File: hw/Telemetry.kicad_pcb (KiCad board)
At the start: 4 copper layers, 100 x 82 mm, 96 parts, among them J101 VS1053 EXP, J102 BOOT0, J103 SPORT, J104 SBUS, J105 USB_B_Micro, J106 UART_EXP, J201 Conn_01x02, J301 Conn_01x02, J302 Conn_01x02, J401 Conn_01x02, J402 Conn_01x02, J403 Conn_01x02, J404 Conn_01x02, J405 Conn_01x02, J406 Conn_01x02, J407 Conn_01x02, J408 Conn_01x02, J409 SERVO_OUT, Q201 AO3401A, Q401 IRLML6344TRPBF, Q402 IRLML6344TRPBF, Q403 IRLML6344TRPBF, Q404 IRLZ44N, Q405 IRLML6344TRPBF, Q406 IRLML6344TRPBF, Q407 IRLML6344TRPBF, Q408 IRLZ44N, SW101 SW_Push, U101 STM32F303CBx, U201 AP1501-K5, U202 RT6200, U301 LF50_TO220, U302 ACS770xCB-100U-PSF, U303 OP179GRT, U304 ACS770xCB-100U-PSF, U305 OP179GRT, X101 TXC-7C

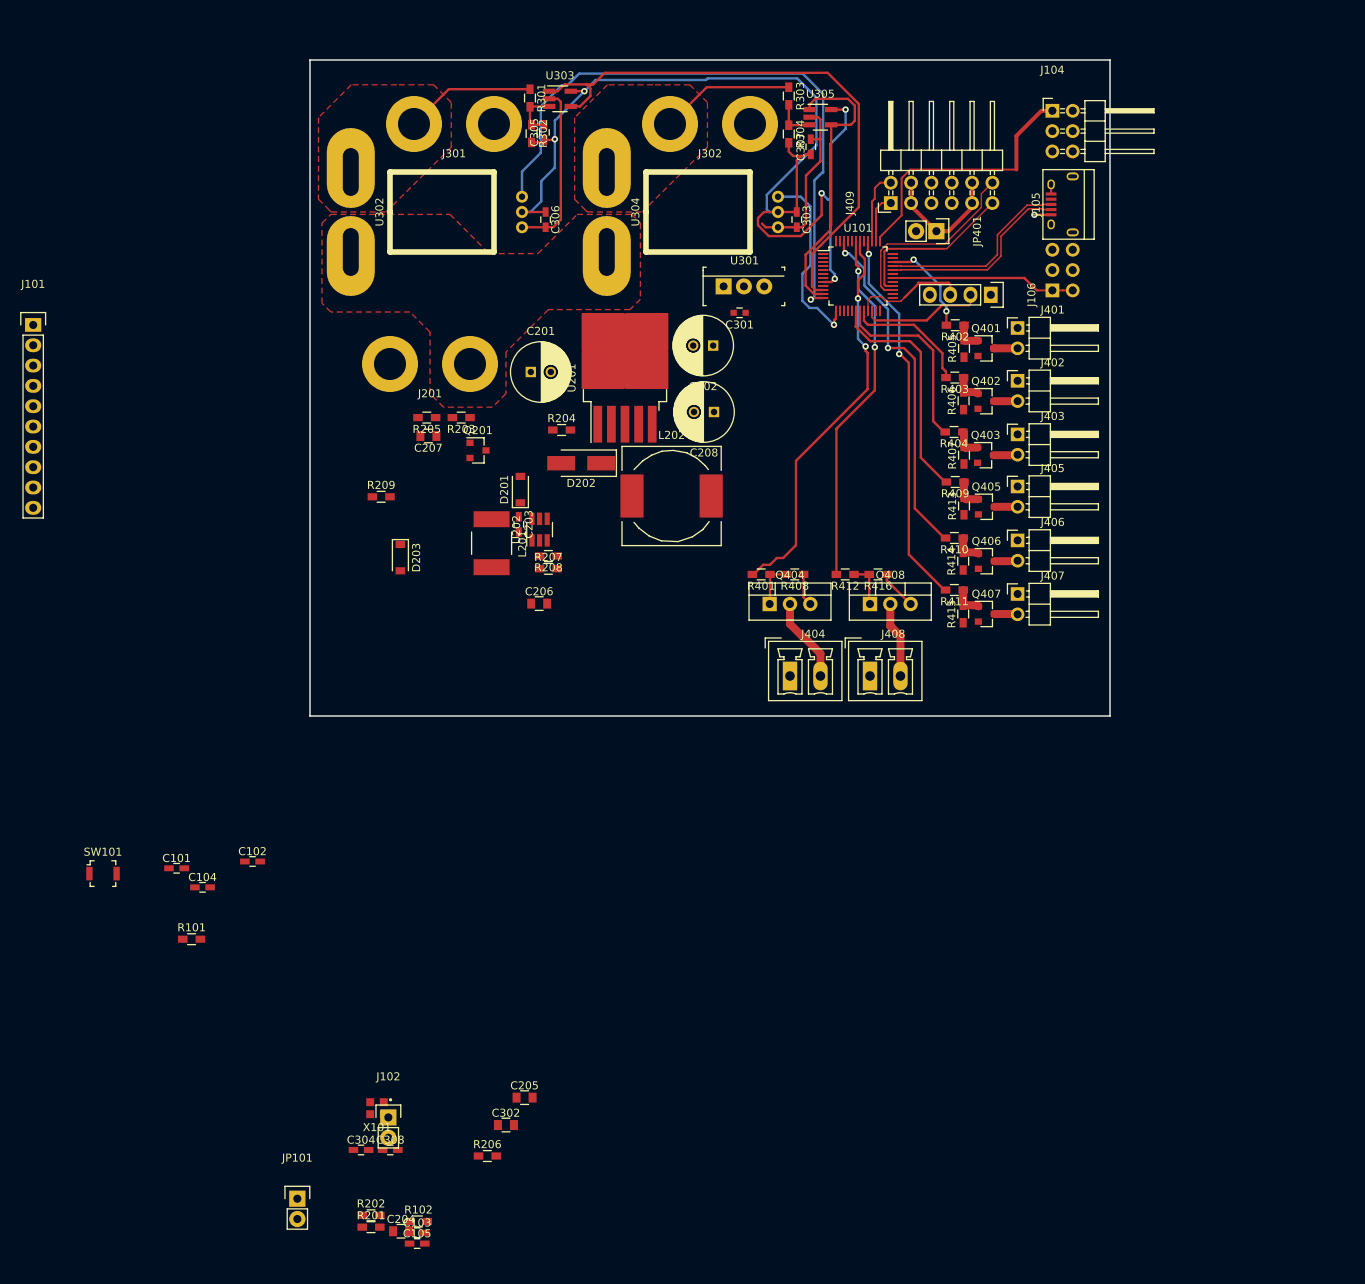
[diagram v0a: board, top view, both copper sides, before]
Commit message: Continued layout Setup USB device CDC
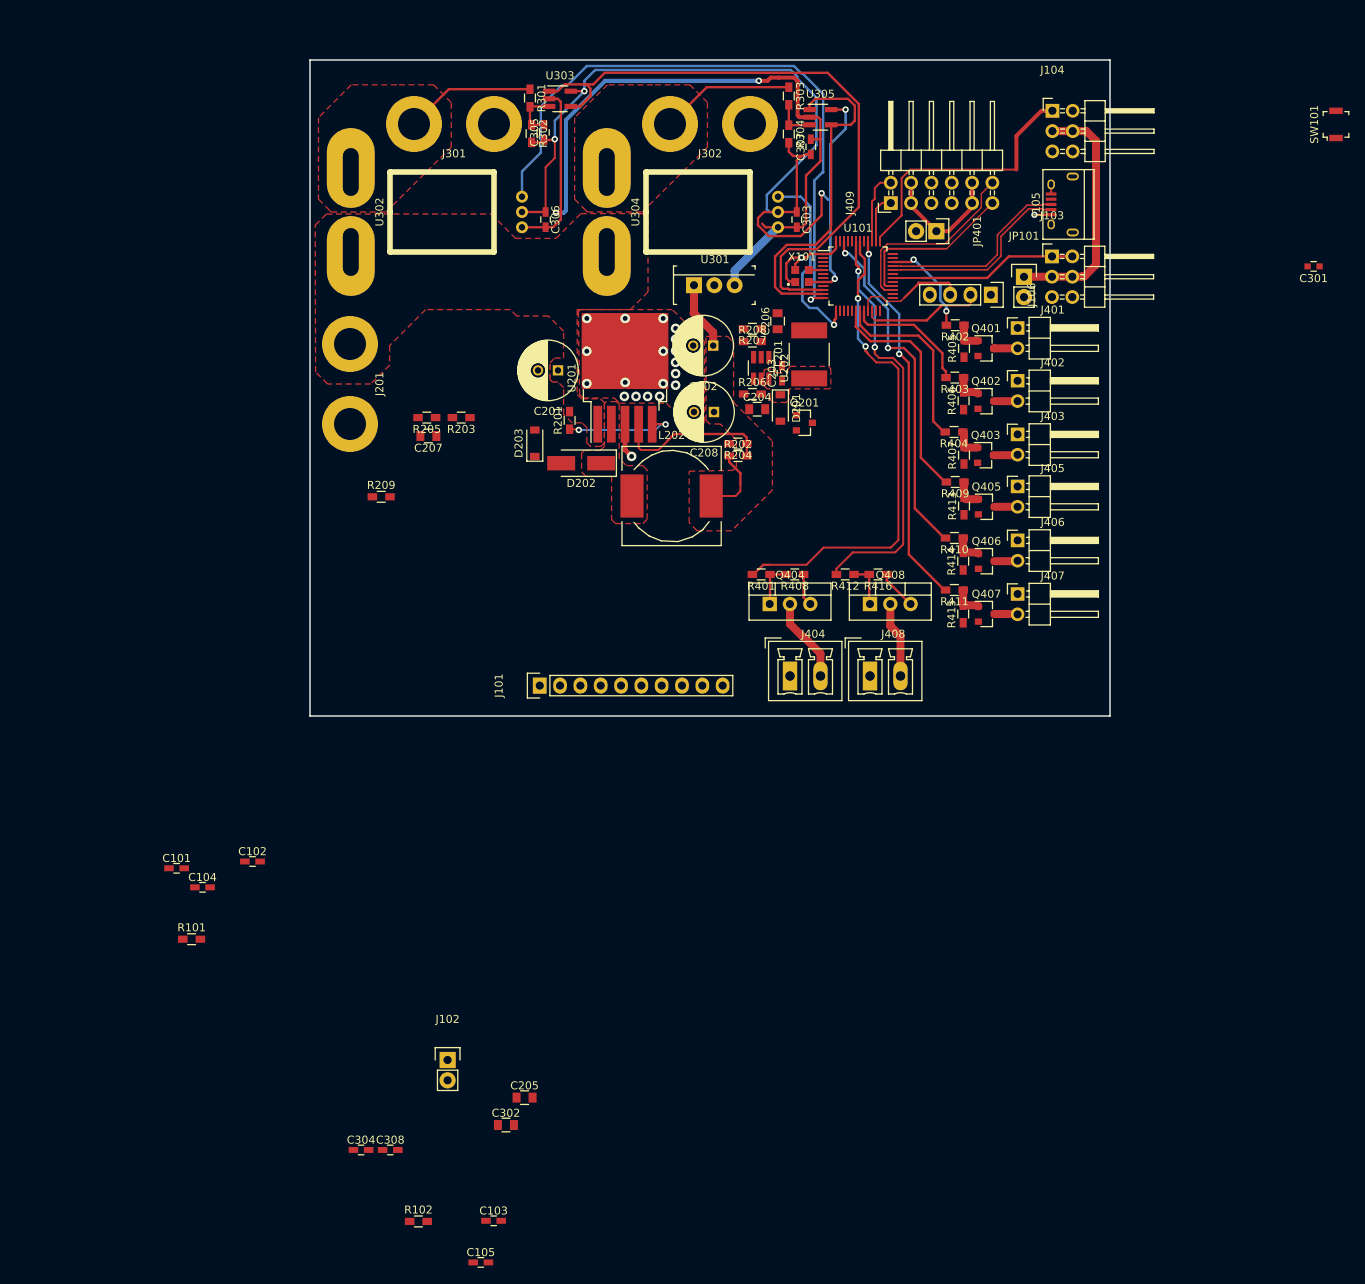
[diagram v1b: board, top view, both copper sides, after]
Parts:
- J103: moved to F.Cu
- moved SW101 180.4 mm to (188.2, 46.0), turned to 90 degrees
- moved JP101 146.7 mm to (149.2, 65.1)
- moved X101 116.8 mm to (121.5, 65.0), turned to 180 degrees
- moved C204 112.0 mm to (115.9, 81.7)
- moved R202 105.4 mm to (113.5, 87.5)
- moved R201 103.9 mm to (92.5, 83.0), turned to 90 degrees
- moved R206 100.9 mm to (115.3, 79.8)
- moved J101 77.7 mm to (88.7, 116.2), turned to 90 degrees
- moved C301 72.0 mm to (185.4, 63.8)
- moved C206 46.2 mm to (118.5, 70.7), turned to 90 degrees
- moved L201 46.2 mm to (122.4, 74.8), turned to 90 degrees
- moved Q201 40.9 mm to (121.8, 83.3)
- moved R207 39.4 mm to (115.3, 71.6), turned to 180 degrees
- moved C203 37.9 mm to (119.0, 77.2), turned to 90 degrees
- moved R208 37.0 mm to (115.3, 73.2), turned to 0 degrees
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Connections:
- U101 pad 1: Net-(R101-Pad1) -> +3V3
- U101 pad 7: (no net) -> Net-(R101-Pad1)
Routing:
- net +5VA: track 43.9 -> 103.9 mm, vias 0 -> 2
- net Net-(J103-Pad3): track 0.00 -> 31.1 mm
- net Net-(R202-Pad2): track 0.00 -> 19.9 mm
- net VCC: track 2.09 -> 19.6 mm
- net Net-(R201-Pad1): track 0.00 -> 14.1 mm, vias 0 -> 2
- net +3V3: track 0.00 -> 13.0 mm, vias 0 -> 1
- net HC_OUT1: track 49.8 -> 61.2 mm
- net ESC1_VOLTAGE_OUT: track 72.7 -> 80.4 mm
- net ESC2_VOLTAGE_OUT: track 36.1 -> 43.8 mm
- net HC_OUT2: track 44.6 -> 51.7 mm
- net GND: track 144.5 -> 150.6 mm, vias 5 -> 24
- net Net-(U101-Pad5): track 0.00 -> 1.83 mm
- net ESC1_CURRENT_OUT: track 78.5 -> 79.3 mm
- added copper zone on F.Cu, net GND
- added copper zone on F.Cu, net Net-(C203-Pad1)
- added copper zone on F.Cu, net Net-(D202-Pad1)
- added copper zone on F.Cu, net VCC

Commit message: Layout improvements
Signed-off-by: findersee <aki.kuusela@findersee.fi>
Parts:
- removed C207: 100n, Capacitors_SMD:C_0805
- removed C305, C308: 100n, Capacitors_SMD:C_0603_HandSoldering
- removed D203: D_Schottky, Diodes_SMD:D_SOD-123
- added C309: 2u2, Capacitors_SMD:C_0805, F.Cu at (106.6, 66.1)
- added Q202: AO3401A, digikey-footprints:SOT-23-3, F.Cu at (112.2, 100.9)
- added Q203: IRLML6344TRPBF, digikey-footprints:SOT-23-3, F.Cu at (87.8, 84.2)
- added Q204: IRLML6344TRPBF, digikey-footprints:SOT-23-3, F.Cu at (83.4, 83.2)
- added R210: 100k, Resistors_SMD:R_0603_HandSoldering, F.Cu at (112.1, 103.8)
- added R211: 10k, Resistors_SMD:R_0603_HandSoldering, F.Cu at (108.0, 100.9)
- added R212: 100k, Resistors_SMD:R_0603_HandSoldering, F.Cu at (83.4, 86.3)
- added R213: 10k, Resistors_SMD:R_0603_HandSoldering, F.Cu at (78.8, 82.3)
- added R214: 100k, Resistors_SMD:R_0603_HandSoldering, F.Cu at (82.4, 79.1)
- added R305: 12k, Resistors_SMD:R_0603_HandSoldering, F.Cu at (88.3, 51.7)
- added R306: 18k, Resistors_SMD:R_0603_HandSoldering, F.Cu at (89.8, 51.7)
- added R307: 12k, Resistors_SMD:R_0603_HandSoldering, F.Cu at (120.5, 53.8)
- added R308: 18k, Resistors_SMD:R_0603_HandSoldering, F.Cu at (122.2, 53.8)
- C204: footprint Capacitors_SMD:C_0805 -> Capacitors_ThroughHole:C_Radial_D7.5_L11.2_P2.5
- C301: value 100n -> 1u
- C302: value 2u2 -> 10n; footprint Capacitors_SMD:C_0805 -> Capacitors_SMD:C_0603_HandSoldering
- J102: footprint Pin_Headers:Pin_Header_Straight_1x02 -> Pin_Headers:Pin_Header_Straight_1x02_Pitch1.00mm
- Q201, Q401, Q402, Q403, Q405, Q406, Q407: footprint TO_SOT_Packages_SMD:SOT-23 -> digikey-footprints:SOT-23-3
- R209: value R_Small -> 100k
- SW101: footprint digikey-footprints:Switch_Tactile_SMD_B3U-1000P -> Pin_Headers:Pin_Header_Straight_1x02_Pitch1.27mm
- U301: value LF50_TO220 -> LP2985-5.0; footprint digikey-footprints:TO-220-3 -> TO_SOT_Packages_SMD:SOT-23-5_HandSoldering
- moved R102 140.4 mm to (127.9, 53.7), turned to 180 degrees
- moved C304 136.3 mm to (90.3, 40.1), turned to 180 degrees
- moved R101 128.5 mm to (128.3, 49.9)
- moved C105 126.9 mm to (120.2, 67.5), turned to 180 degrees
- moved C103 124.4 mm to (135.9, 70.5)
- moved J102 117.6 mm to (128.3, 57.1), turned to 180 degrees
- moved C104 116.6 mm to (126.7, 56.6), turned to 90 degrees
- moved C102 114.8 mm to (139.3, 62.7)
- moved C302 110.4 mm to (111.0, 64.0), turned to 180 degrees
- moved C101 104.4 mm to (117.4, 65.4), turned to 270 degrees
- moved C205 81.9 mm to (123.1, 94.3)
- moved C301 73.6 mm to (112.0, 68.0), turned to 270 degrees
- moved SW101 61.5 mm to (127.0, 51.7)
- moved J404 51.7 mm to (68.3, 115.0)
- moved Q408 51.7 mm to (78.3, 106.0)
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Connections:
- C204 pad 1: Net-(C204-Pad1) -> +BATT
- C205 pad 1: Net-(C204-Pad1) -> +BATT
- C302 pad 1: +5VA -> Net-(C302-Pad1)
- J105 pad 1: VCC -> VBUS
- Q201 pad 2: Net-(C204-Pad1) -> +BATT
- Q201 pad 3: VCC -> VBUS
- R206 pad 2: Net-(C204-Pad1) -> +BATT
- U202 pad 5: Net-(C204-Pad1) -> +BATT
- U301 pad 3: +5VA -> VCC
- U302 pad 3: ESC1_CURRENT_OUT -> Net-(R305-Pad2)
- U304 pad 3: ESC2_CURRENT_OUT -> Net-(R307-Pad2)
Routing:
- net +BATT: track 0.00 -> 137.1 mm, vias 0 -> 1
- net VBUS: track 0.00 -> 136.0 mm, vias 0 -> 4
- net HC_OUT1: track 61.2 -> 143.7 mm
- net BAT_VOLTAGE: track 0.00 -> 65.3 mm, vias 0 -> 2
- net HC_OUT2: track 51.7 -> 111.7 mm
- net /XCS: track 0.00 -> 57.7 mm, vias 0 -> 1
- net /SPI_CS: track 0.00 -> 55.6 mm
- net /SPI_MISO: track 0.00 -> 54.1 mm
- net /XRESET: track 0.00 -> 53.8 mm, vias 0 -> 1
- net /XDCS: track 0.00 -> 52.8 mm, vias 0 -> 1
- net /SPI_MOSI: track 0.00 -> 52.6 mm
- net GND: track 150.6 -> 203.1 mm, vias 24 -> 46
- net /DREQ: track 0.00 -> 49.8 mm, vias 0 -> 2
- net /SPI_SCK: track 0.00 -> 49.6 mm, vias 0 -> 1
- net Net-(Q203-Pad1): track 0.00 -> 35.4 mm
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- added copper zone on F.Cu, net +3V3
- added copper zone on In2.Cu, net +3V3
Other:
- net class Default: via_dia 0.8 -> 0.65; via_drill 0.4 -> 0.3
- rule via_min_size: 0.4 -> 0.45

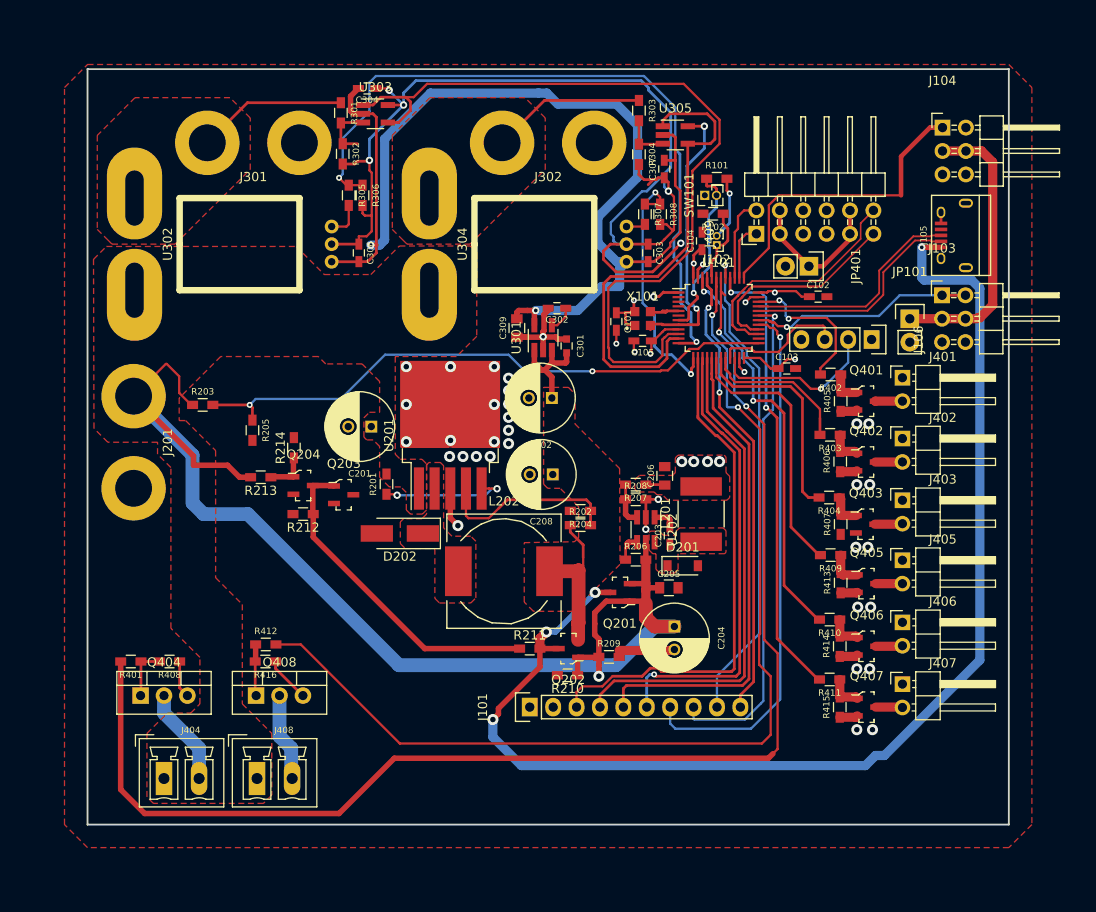
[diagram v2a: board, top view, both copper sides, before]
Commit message: Added DAC initialization Added 32Mbit SPI FLASH memory Removed SPI expansion port
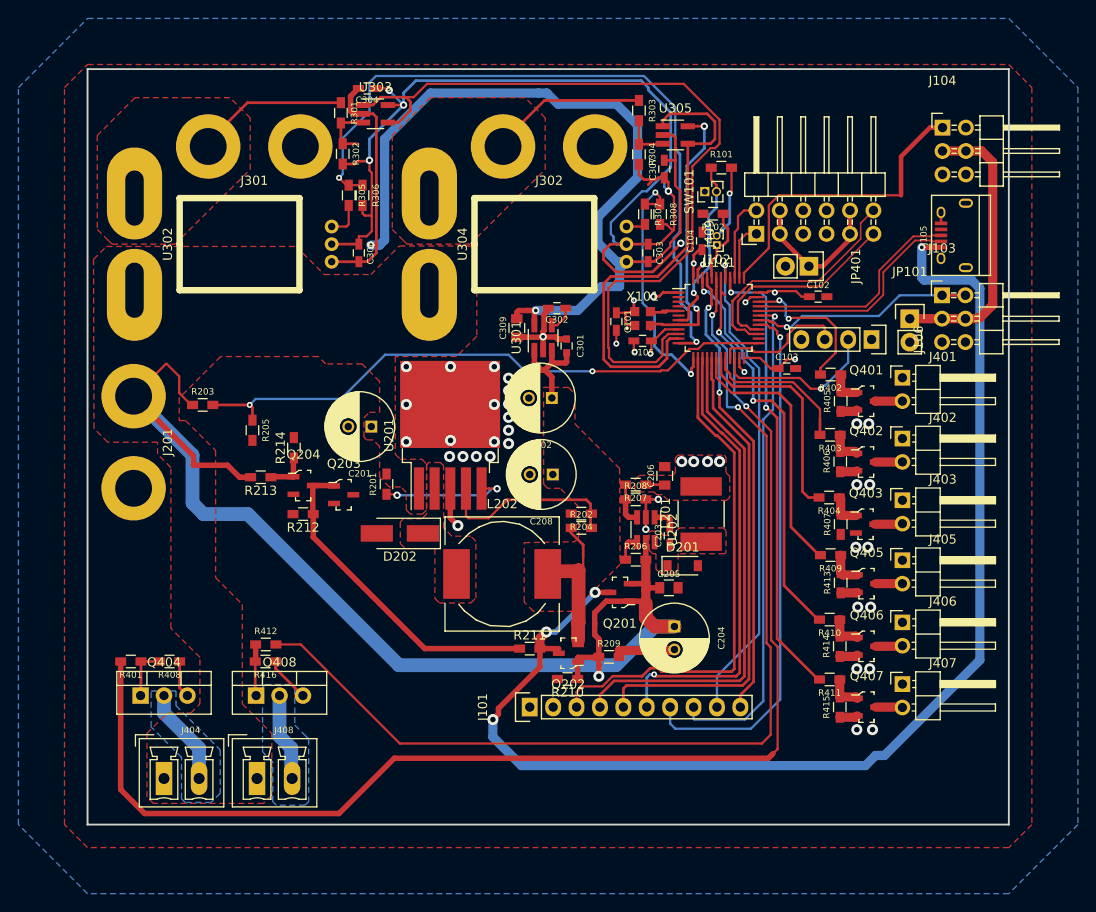
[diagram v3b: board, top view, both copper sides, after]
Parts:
- moved R101 1.30 mm to (128.8, 48.7)
- moved Q202 0.50 mm to (112.2, 101.4)
- moved J301 0.41 mm to (78.1, 46.4)
- moved J302 0.41 mm to (110.1, 46.4)
- moved R210 0.40 mm to (112.1, 104.2)
- moved SW101 0.40 mm to (127.0, 51.3)
- moved L202 0.36 mm to (105.0, 92.8)
- moved R202 0.32 mm to (113.6, 87.8)
- moved R204 0.32 mm to (113.6, 86.2)
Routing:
- net +3V3: track 38.4 -> 39.6 mm
- net Net-(R101-Pad1): track 19.1 -> 19.9 mm
- added copper zone on B.Cu, net GND
- added copper zone on B.Cu, net Net-(J404-Pad2)
- added copper zone on B.Cu, net Net-(J408-Pad2)
